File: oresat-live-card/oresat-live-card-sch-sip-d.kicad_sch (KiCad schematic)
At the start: 7 parts, among them J3 Conn_01x02, U7 OSD3358-512M-BSM

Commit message: Changed to hierarchy view
updated OPD and component symbols. Resolved all DRC errors and warnings.
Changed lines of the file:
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@@
 		)
 	)
-	(global_label "TRANSMIT"
+	(hierarchical_label "TRANSMIT"
 		(shape output)
 		(at 120.65 111.76 180)
-		(fields_autoplaced yes)
 		(effects
 			(font
@@
 			(justify right)
 		)
-		(property "Intersheetrefs" "${INTERSHEET_REFS}"
-			(at 108.7748 111.76 0)
-			(show_name no)
-			(do_not_autoplace no)
-			(effects
-				(font
-					(size 0.9601 0.9601)
-				)
-				(justify right)
-			)
-		)
 	)
-	(global_label "SYSBOOT2"
-		(shape input)
+	(hierarchical_label "SYSBOOT2"
+		(shape output)
 		(at 295.91 116.84 0)
-		(fields_autoplaced yes)
 		(effects
 			(font
@@
 			(justify left)
 		)
-		(property "Intersheetrefs" "${INTERSHEET_REFS}"
-			(at 308.5109 116.84 0)
-			(show_name no)
-			(do_not_autoplace no)
-			(effects
-				(font
-					(size 1.27 1.27)
-				)
-				(justify left)
-			)
-		)
 	)
-	(global_label "ANT_SEL"
+	(hierarchical_label "ANT_SEL"
 		(shape output)
 		(at 120.65 114.3 180)
-		(fields_autoplaced yes)
 		(effects
 			(font
@@
 			(justify right)
 		)
-		(property "Intersheetrefs" "${INTERSHEET_REFS}"
-			(at 109.9239 114.3 0)
-			(show_name no)
-			(do_not_autoplace no)
-			(effects
-				(font
-					(size 1.27 1.27)
-				)
-				(justify right)
-			)
-		)
 	)

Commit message: Organizational changes
Updated hierarchical labels and other misc schematic fixes
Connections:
- net TRANSMIT renamed TX/RX_SWITCH
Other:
- moved on the sheet: TP11, TP25
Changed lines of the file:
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@@
+	)
+	(junction
+		(at 127 111.76)
+		(diameter 0)
+		(color 0 0 0 0)
 	)
 	(junction
@@
 	)
 	(junction
-		(at 127 111.76)
-		(diameter 0)
-		(color 0 0 0 0)
-	)
-	(junction
 		(at 237.49 172.72)
 		(diameter 0)
@@
 	(wire
 		(pts
-			(xy 127 114.3) (xy 127 119.38)
-		)
-		(stroke
-			(width 0)
-			(type default)
-		)
-	)
-	(wire
-		(pts
 			(xy 196.85 132.08) (xy 219.71 132.08)
 		)
@@
 	(wire
 		(pts
+			(xy 127 114.3) (xy 135.89 114.3)
+		)
+		(stroke
+			(width 0)
+			(type default)
+		)
+	)
+	(wire
+		(pts
 			(xy 224.79 170.18) (xy 224.79 172.72)
 		)
@@
 	(wire
 		(pts
+			(xy 127 111.76) (xy 135.89 111.76)
+		)
+		(stroke
+			(width 0)
+			(type default)
+		)
+	)
+	(wire
+		(pts
 			(xy 196.85 149.86) (xy 234.95 149.86)
 		)
@@
 	(wire
 		(pts
-			(xy 127 106.68) (xy 127 111.76)
-		)
-		(stroke
-			(width 0)
-			(type default)
-		)
-	)
-	(wire
-		(pts
 			(xy 196.85 134.62) (xy 222.25 134.62)
 		)
@@
 	(wire
 		(pts
-			(xy 127 114.3) (xy 135.89 114.3)
-		)
-		(stroke
-			(width 0)
-			(type default)
-		)
-	)
-	(wire
-		(pts
 			(xy 275.59 97.79) (xy 275.59 121.92)
 		)
@@
 	(wire
 		(pts
-			(xy 135.89 111.76) (xy 127 111.76)
-		)
-		(stroke
-			(width 0)
-			(type default)
-		)
-	)
-	(wire
-		(pts
-			(xy 127 111.76) (xy 120.65 111.76)
+			(xy 120.65 111.76) (xy 127 111.76)
 		)
 		(stroke
@@
 		)
 	)
-	(hierarchical_label "TRANSMIT"
+	(hierarchical_label "TX{slash}RX_SWITCH"
 		(shape output)
 		(at 120.65 111.76 180)
@@
 	(symbol
 		(lib_id "oresat-misc:Test-Point-1mm-round")
-		(at 127 106.68 90)
+		(at 127 111.76 90)
 		(unit 1)
 		(body_style 1)
@@
 		(dnp no)
 		(property "Reference" "TP11"
-			(at 125.73 105.41 90)
+			(at 129.794 107.696 90)
 			(show_name no)
 			(do_not_autoplace no)
@@
 		)
 		(property "Value" "TEST-POINT3X4"
-			(at 129.54 109.22 0)
+			(at 129.54 114.3 0)
 			(hide yes)
 			(show_name no)
@@
 		)
 		(property "Footprint" "oresat-misc:TestPoint_Pad_D1.0mm"
-			(at 116.84 106.68 0)
+			(at 116.84 111.76 0)
 			(hide yes)
 			(show_name no)
@@
 		)
 		(property "Datasheet" ""
-			(at 127 106.68 0)
+			(at 127 111.76 0)
 			(hide yes)
 			(show_name no)
@@
 		)
 		(property "Description" ""
-			(at 127 106.68 0)
+			(at 127 111.76 0)
 			(hide yes)
 			(show_name no)
@@
 		)
 		(property "DIS" ""
-			(at 127 106.68 90)
+			(at 127 111.76 90)
 			(hide yes)
 			(show_name no)
@@
 	(symbol
 		(lib_id "oresat-misc:Test-Point-1mm-round")
-		(at 127 119.38 90)
+		(at 127 114.3 180)
 		(unit 1)
 		(body_style 1)
@@
 		(dnp no)
 		(property "Reference" "TP25"
-			(at 125.73 118.11 90)
+			(at 129.286 116.84 0)
 			(show_name no)
 			(do_not_autoplace no)
@@
 		)
 		(property "Value" "TEST-POINT3X4"
-			(at 129.54 121.92 0)
+			(at 129.54 111.76 0)
 			(hide yes)
 			(show_name no)
@@
 		)
 		(property "Footprint" "oresat-misc:TestPoint_Pad_D1.0mm"
-			(at 116.84 119.38 0)
+			(at 127 124.46 0)
 			(hide yes)
 			(show_name no)
@@
 		)
 		(property "Datasheet" ""
-			(at 127 119.38 0)
+			(at 127 114.3 0)
 			(hide yes)
 			(show_name no)
@@
 		)
 		(property "Description" ""
-			(at 127 119.38 0)
+			(at 127 114.3 0)
 			(hide yes)
 			(show_name no)
@@
 		)
 		(property "DIS" ""
-			(at 127 119.38 90)
+			(at 127 114.3 90)
 			(hide yes)
 			(show_name no)

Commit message: BOM changes
Updated components outside of RF path to on hand parts.
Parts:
- R24, R25, R26: value 100k -> 665k; footprint oresat-live-card:ARRAY_EXBA-M -> oresat-passives:0603-C-NOSILK; DPN U7104CT-ND -> RMCF0603FT665KCT-ND; MFR Panasonic -> Stackpole Electronics; MPN EXB-A10P104J -> RMCF0603FT665K
- TP11, TP25: footprint oresat-misc:TestPoint_Pad_D1.0mm -> oresat-misc:TestPoint-0.75mm-th
- U7: value OSD3358-512M-BSM -> TPS2041BQDBVRQ1; footprint oresat-ics:U-Octavo-OSD335X-BGA-256 -> oresat-live-card:DBV5; DPN 1676-1002-ND -> 296-25159-1-ND; MFR Octavo Systems -> Texas Instruments; MPN OSD3358-512M-BSM -> TPS2041BQDBVRQ1
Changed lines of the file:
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@@
 			)
 		)
-		(property "Footprint" "oresat-misc:TestPoint_Pad_D1.0mm"
+		(property "Footprint" "oresat-misc:TestPoint-0.75mm-th"
 			(at 116.84 111.76 0)
 			(hide yes)
@@
 			)
 		)
-		(property "Footprint" "oresat-misc:TestPoint_Pad_D1.0mm"
+		(property "Footprint" "oresat-misc:TestPoint-0.75mm-th"
 			(at 127 124.46 0)
 			(hide yes)
@@
 			)
 		)
-		(property "Value" "100k"
+		(property "Value" "665k"
 			(at 264.16 81.026 90)
 			(show_name no)
@@
 			)
 		)
-		(property "Footprint" "oresat-live-card:ARRAY_EXBA-M"
+		(property "Footprint" "oresat-passives:0603-C-NOSILK"
 			(at 257.81 85.09 0)
 			(hide yes)
@@
 			)
 		)
-		(property "Datasheet" ""
+		(property "Datasheet" "https://www.seielect.com/catalog/SEI-RMCF_RMCP.pdf"
 			(at 257.81 85.09 0)
 			(hide yes)
@@
 			)
 		)
-		(property "Description" "RES ARRAY 8 RES 100K OHM 2512"
+		(property "Description" "665 kOhms ±1% 0.1W, 1/10W Chip Resistor 0603 (1608 Metric) Automotive AEC-Q200 Thick Film"
 			(at 257.81 85.09 0)
 			(hide yes)
@@
 			)
 		)
-		(property "MPN" "EXB-A10P104J"
+		(property "MPN" "RMCF0603FT665K"
 			(at 257.81 85.09 0)
 			(hide yes)
@@
 			)
 		)
-		(property "DPN" "U7104CT-ND "
+		(property "DPN" "RMCF0603FT665KCT-ND"
 			(at 257.81 85.09 90)
 			(hide yes)
@@
 			)
 		)
-		(property "MFR" "Panasonic "
+		(property "MFR" "Stackpole Electronics"
 			(at 257.81 85.09 90)
 			(hide yes)
@@
 			)
 		)
-		(property "Value" "OSD3358-512M-BSM"
+		(property "Value" "TPS2041BQDBVRQ1"
 			(at 140.97 104.14 0)
 			(show_name no)
@@
 			)
 		)
-		(property "Footprint" "oresat-ics:U-Octavo-OSD335X-BGA-256"
+		(property "Footprint" "oresat-live-card:DBV5"
 			(at 166.37 31.75 0)
 			(hide yes)
@@
 			)
 		)
-		(property "Datasheet" ""
+		(property "Datasheet" "https://www.ti.com/lit/ds/symlink/tps2041b-q1.pdf?HQS=dis-dk-null-digikeymode-dsf-pf-null-wwe&ts=1651525711603&ref_url=https%253A%252F%252Fwww.ti.com%252Fgeneral%252Fdocs%252Fsuppproductinfo.tsp%253FdistId%253D10%2526gotoUrl%253Dhttps%253A%252F%252Fwww.ti.com%252Flit%252Fgpn%252Ftps2041b-q1"
 			(at 166.37 139.7 0)
 			(hide yes)
@@
 			)
 		)
-		(property "Description" "OSD335x Embedded Module 1GHz 512MB"
+		(property "Description" "Power Switch/Driver 1:1 N-Channel 500mA"
 			(at 166.37 139.7 0)
 			(hide yes)
@@
 			)
 		)
-		(property "MPN" "OSD3358-512M-BSM"
+		(property "MPN" "TPS2041BQDBVRQ1"
 			(at 166.37 139.7 0)
 			(hide yes)
@@
 			)
 		)
-		(property "DPN" "1676-1002-ND "
+		(property "DPN" "296-25159-1-ND "
 			(at 166.37 139.7 0)
 			(hide yes)
@@
 			)
 		)
-		(property "MFR" "Octavo Systems "
+		(property "MFR" "Texas Instruments "
 			(at 166.37 139.7 0)
 			(hide yes)
@@
 			)
 		)
-		(property "Value" "100k"
+		(property "Value" "665k"
 			(at 216.662 172.72 90)
 			(show_name no)
@@
 			)
 		)
-		(property "Footprint" "oresat-live-card:ARRAY_EXBA-M"
+		(property "Footprint" "oresat-passives:0603-C-NOSILK"
 			(at 234.95 167.64 0)
 			(hide yes)
@@
 			)
 		)
-		(property "Datasheet" ""
+		(property "Datasheet" "https://www.seielect.com/catalog/SEI-RMCF_RMCP.pdf"
 			(at 234.95 167.64 0)
 			(hide yes)
@@
 			)
 		)
-		(property "Description" "RES ARRAY 8 RES 100K OHM 2512"
+		(property "Description" "665 kOhms ±1% 0.1W, 1/10W Chip Resistor 0603 (1608 Metric) Automotive AEC-Q200 Thick Film"
 			(at 234.95 167.64 0)
 			(hide yes)
@@
 			)
 		)
-		(property "MPN" "EXB-A10P104J"
+		(property "MPN" "RMCF0603FT665K"
 			(at 234.95 167.64 0)
 			(hide yes)
@@
 			)
 		)
-		(property "DPN" "U7104CT-ND "
+		(property "DPN" "RMCF0603FT665KCT-ND"
 			(at 234.95 167.64 90)
 			(hide yes)
@@
 			)
 		)
-		(property "MFR" "Panasonic "
+		(property "MFR" "Stackpole Electronics"
 			(at 234.95 167.64 90)
 			(hide yes)
@@
 			)
 		)
-		(property "Value" "100k"
+		(property "Value" "665k"
 			(at 260.35 172.466 90)
 			(show_name no)
@@
 			)
 		)
-		(property "Footprint" "oresat-live-card:ARRAY_EXBA-M"
+		(property "Footprint" "oresat-passives:0603-C-NOSILK"
 			(at 260.35 167.64 0)
 			(hide yes)
@@
 			)
 		)
-		(property "Datasheet" ""
+		(property "Datasheet" "https://www.seielect.com/catalog/SEI-RMCF_RMCP.pdf"
 			(at 260.35 167.64 0)
 			(hide yes)
@@
 			)
 		)
-		(property "Description" "RES ARRAY 8 RES 100K OHM 2512"
+		(property "Description" "665 kOhms ±1% 0.1W, 1/10W Chip Resistor 0603 (1608 Metric) Automotive AEC-Q200 Thick Film"
 			(at 260.35 167.64 0)
 			(hide yes)
@@
 			)
 		)
-		(property "MPN" "EXB-A10P104J"
+		(property "MPN" "RMCF0603FT665K"
 			(at 260.35 167.64 0)
 			(hide yes)
@@
 			)
 		)
-		(property "DPN" "U7104CT-ND "
+		(property "DPN" "RMCF0603FT665KCT-ND"
 			(at 260.35 167.64 90)
 			(hide yes)
@@
 			)
 		)
-		(property "MFR" "Panasonic "
+		(property "MFR" "Stackpole Electronics"
 			(at 260.35 167.64 90)
 			(hide yes)

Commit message: BOM changed to match older version
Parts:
- R24, R25, R26: value 665k -> 100k; footprint oresat-passives:0603-C-NOSILK -> oresat-live-card:ARRAY_EXBA-M; DPN RMCF0603FT665KCT-ND -> U7104CT-ND; MFR Stackpole Electronics -> Panasonic; MPN RMCF0603FT665K -> EXB-A10P104J
- TP11, TP25: footprint oresat-misc:TestPoint-0.75mm-th -> oresat-misc:TestPoint_Pad_D1.0mm
- U7: value TPS2041BQDBVRQ1 -> OSD3358-512M-BSM; footprint oresat-live-card:DBV5 -> oresat-ics:U-Octavo-OSD335X-BGA-256; DPN 296-25159-1-ND -> 1676-1002-ND; MFR Texas Instruments -> Octavo Systems; MPN TPS2041BQDBVRQ1 -> OSD3358-512M-BSM
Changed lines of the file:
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@@
 			)
 		)
-		(property "Footprint" "oresat-misc:TestPoint-0.75mm-th"
+		(property "Footprint" "oresat-misc:TestPoint_Pad_D1.0mm"
 			(at 116.84 111.76 0)
 			(hide yes)
@@
 			)
 		)
-		(property "Footprint" "oresat-misc:TestPoint-0.75mm-th"
+		(property "Footprint" "oresat-misc:TestPoint_Pad_D1.0mm"
 			(at 127 124.46 0)
 			(hide yes)
@@
 			)
 		)
-		(property "Value" "665k"
+		(property "Value" "100k"
 			(at 264.16 81.026 90)
 			(show_name no)
@@
 			)
 		)
-		(property "Footprint" "oresat-passives:0603-C-NOSILK"
+		(property "Footprint" "oresat-live-card:ARRAY_EXBA-M"
 			(at 257.81 85.09 0)
 			(hide yes)
@@
 			)
 		)
-		(property "Description" "665 kOhms ±1% 0.1W, 1/10W Chip Resistor 0603 (1608 Metric) Automotive AEC-Q200 Thick Film"
+		(property "Description" "RES ARRAY 8 RES 100K OHM 2512"
 			(at 257.81 85.09 0)
 			(hide yes)
@@
 			)
 		)
-		(property "MPN" "RMCF0603FT665K"
+		(property "MPN" "EXB-A10P104J"
 			(at 257.81 85.09 0)
 			(hide yes)
@@
 			)
 		)
-		(property "DPN" "RMCF0603FT665KCT-ND"
+		(property "DPN" "U7104CT-ND"
 			(at 257.81 85.09 90)
 			(hide yes)
@@
 			)
 		)
-		(property "MFR" "Stackpole Electronics"
+		(property "MFR" "Panasonic"
 			(at 257.81 85.09 90)
 			(hide yes)
@@
 			)
 		)
-		(property "Value" "TPS2041BQDBVRQ1"
+		(property "Value" "OSD3358-512M-BSM"
 			(at 140.97 104.14 0)
 			(show_name no)
@@
 			)
 		)
-		(property "Footprint" "oresat-live-card:DBV5"
+		(property "Footprint" "oresat-ics:U-Octavo-OSD335X-BGA-256"
 			(at 166.37 31.75 0)
 			(hide yes)
@@
 			)
 		)
-		(property "Description" "Power Switch/Driver 1:1 N-Channel 500mA"
+		(property "Description" "OSD335x Embedded Module 1GHz 512MB"
 			(at 166.37 139.7 0)
 			(hide yes)
@@
 			)
 		)
-		(property "MPN" "TPS2041BQDBVRQ1"
+		(property "MPN" "OSD3358-512M-BSM"
 			(at 166.37 139.7 0)
 			(hide yes)
@@
 			)
 		)
-		(property "DPN" "296-25159-1-ND "
+		(property "DPN" "1676-1002-ND"
 			(at 166.37 139.7 0)
 			(hide yes)
@@
 			)
 		)
-		(property "MFR" "Texas Instruments "
+		(property "MFR" "Octavo Systems"
 			(at 166.37 139.7 0)
 			(hide yes)
@@
 			)
 		)
-		(property "Value" "665k"
+		(property "Value" "100k"
 			(at 216.662 172.72 90)
 			(show_name no)
@@
 			)
 		)
-		(property "Footprint" "oresat-passives:0603-C-NOSILK"
+		(property "Footprint" "oresat-live-card:ARRAY_EXBA-M"
 			(at 234.95 167.64 0)
 			(hide yes)
@@
 			)
 		)
-		(property "Description" "665 kOhms ±1% 0.1W, 1/10W Chip Resistor 0603 (1608 Metric) Automotive AEC-Q200 Thick Film"
+		(property "Description" "RES ARRAY 8 RES 100K OHM 2512"
 			(at 234.95 167.64 0)
 			(hide yes)
@@
 			)
 		)
-		(property "MPN" "RMCF0603FT665K"
+		(property "MPN" "EXB-A10P104J"
 			(at 234.95 167.64 0)
 			(hide yes)
@@
 			)
 		)
-		(property "DPN" "RMCF0603FT665KCT-ND"
+		(property "DPN" "U7104CT-ND"
 			(at 234.95 167.64 90)
 			(hide yes)
@@
 			)
 		)
-		(property "MFR" "Stackpole Electronics"
+		(property "MFR" "Panasonic"
 			(at 234.95 167.64 90)
 			(hide yes)
@@
 			)
 		)
-		(property "Value" "665k"
+		(property "Value" "100k"
 			(at 260.35 172.466 90)
 			(show_name no)
@@
 			)
 		)
-		(property "Footprint" "oresat-passives:0603-C-NOSILK"
+		(property "Footprint" "oresat-live-card:ARRAY_EXBA-M"
 			(at 260.35 167.64 0)
 			(hide yes)
@@
 			)
 		)
-		(property "Description" "665 kOhms ±1% 0.1W, 1/10W Chip Resistor 0603 (1608 Metric) Automotive AEC-Q200 Thick Film"
+		(property "Description" "RES ARRAY 8 RES 100K OHM 2512"
 			(at 260.35 167.64 0)
 			(hide yes)
@@
 			)
 		)
-		(property "MPN" "RMCF0603FT665K"
+		(property "MPN" "EXB-A10P104J"
 			(at 260.35 167.64 0)
 			(hide yes)
@@
 			)
 		)
-		(property "DPN" "RMCF0603FT665KCT-ND"
+		(property "DPN" "U7104CT-ND"
 			(at 260.35 167.64 90)
 			(hide yes)
@@
 			)
 		)
-		(property "MFR" "Stackpole Electronics"
+		(property "MFR" "Panasonic"
 			(at 260.35 167.64 90)
 			(hide yes)

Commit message: mostly just polish after BOM fixes
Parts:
- TP11, TP25: now left out of the parts list
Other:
- note added: "All resistors 0603 +/- 1% unless marked and AEQ certified unless otherwise marked. All caps are 0603 10% X5R or better and Vw >= 25 V and AEQ certified unless otherwise marked."
- note removed: "All caps are 0603 ceramic 10% X7R Vw>=16V unless marked"
- note removed: "All resistors 0603 +/- 1% unless marked"
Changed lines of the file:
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@@
+		)
+	)
+	(text "All resistors 0603 +/- 1% unless marked and AEQ certified unless otherwise marked.\nAll caps are 0603 10% X5R or better and Vw >= 25 V and AEQ certified unless otherwise marked."
+		(exclude_from_sim no)
+		(at 113.284 265.43 0)
+		(effects
+			(font
+				(size 1.778 1.5113)
+			)
+			(justify left bottom)
 		)
 	)
@@
 		(effects
 			(font
-				(size 1.778 1.5113)
+				(size 1.27 1.27)
 			)
 			(justify left bottom)
@@
 		(exclude_from_sim no)
 		(at 222.25 187.96 0)
-		(effects
-			(font
-				(size 1.778 1.5113)
-			)
-			(justify left bottom)
-		)
-	)
-	(text "All caps are 0603 ceramic 10% X7R Vw>=16V unless marked"
-		(exclude_from_sim no)
-		(at 119.38 264.16 0)
 		(effects
 			(font
@@
 				(thickness 0.6)
 				(bold yes)
-			)
-			(justify left bottom)
-		)
-	)
-	(text "All resistors 0603 +/- 1% unless marked"
-		(exclude_from_sim no)
-		(at 119.38 261.62 0)
-		(effects
-			(font
-				(size 1.778 1.5113)
 			)
 			(justify left bottom)
@@
 		(body_style 1)
 		(exclude_from_sim no)
-		(in_bom yes)
+		(in_bom no)
 		(on_board yes)
 		(in_pos_files yes)
@@
 		(body_style 1)
 		(exclude_from_sim no)
-		(in_bom yes)
+		(in_bom no)
 		(on_board yes)
 		(in_pos_files yes)

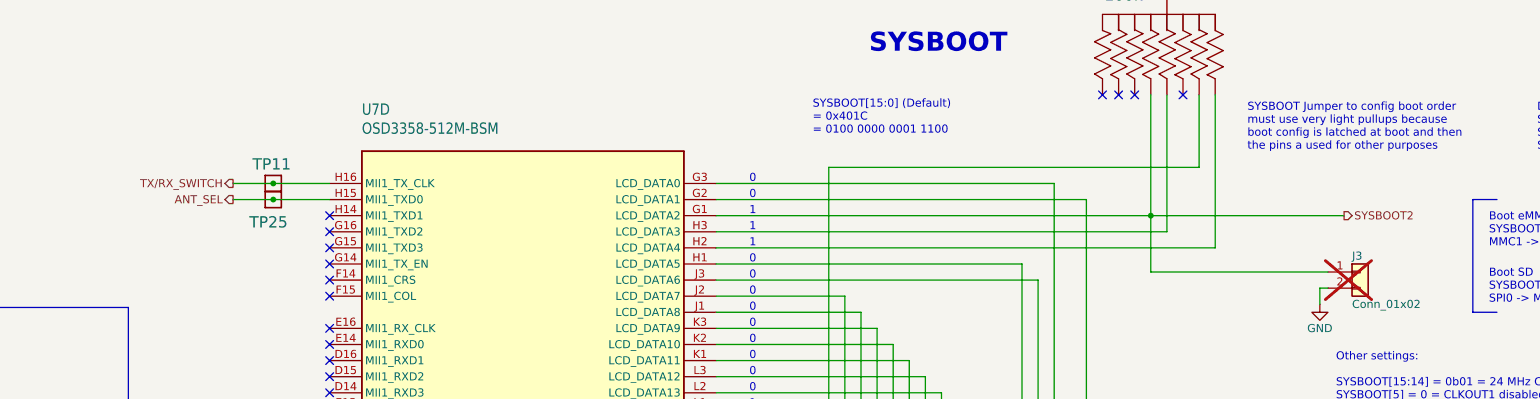
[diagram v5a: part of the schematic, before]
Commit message: More schematic cleanup, sync between sch/brd, and some board cleanup. No more DRCs.
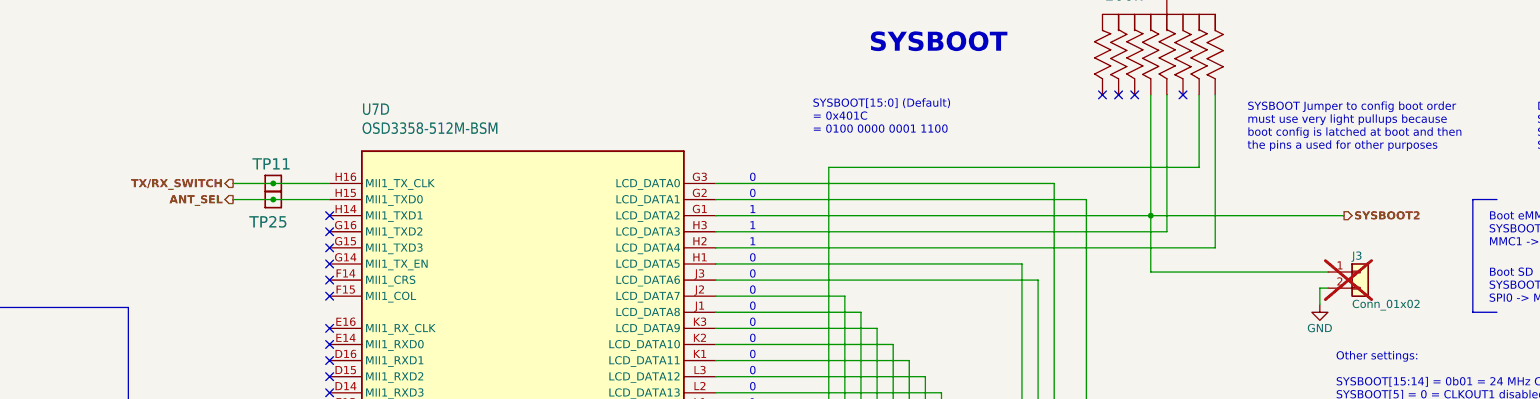
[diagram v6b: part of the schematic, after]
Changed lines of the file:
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@@
 			(font
 				(size 1.27 1.27)
+				(thickness 0.254)
+				(bold yes)
 			)
 			(justify right)
@@
 			(font
 				(size 1.27 1.27)
+				(thickness 0.254)
+				(bold yes)
 			)
 			(justify left)
@@
 			(font
 				(size 1.27 1.27)
+				(thickness 0.254)
+				(bold yes)
 			)
 			(justify right)
